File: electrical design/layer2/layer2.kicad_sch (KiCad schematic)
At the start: 36 parts, among them J1 Conn_01x01_Female, J10 Conn_01x01_Female, J2 Conn_01x01_Female, J3 Conn_01x01_Female, J4 Conn_01x01_Female, J5 Conn_01x01_Female, J6 Conn_01x01_Female, J7 Conn_01x01_Female, J8 Conn_01x01_Female, J9 Conn_01x01_Female

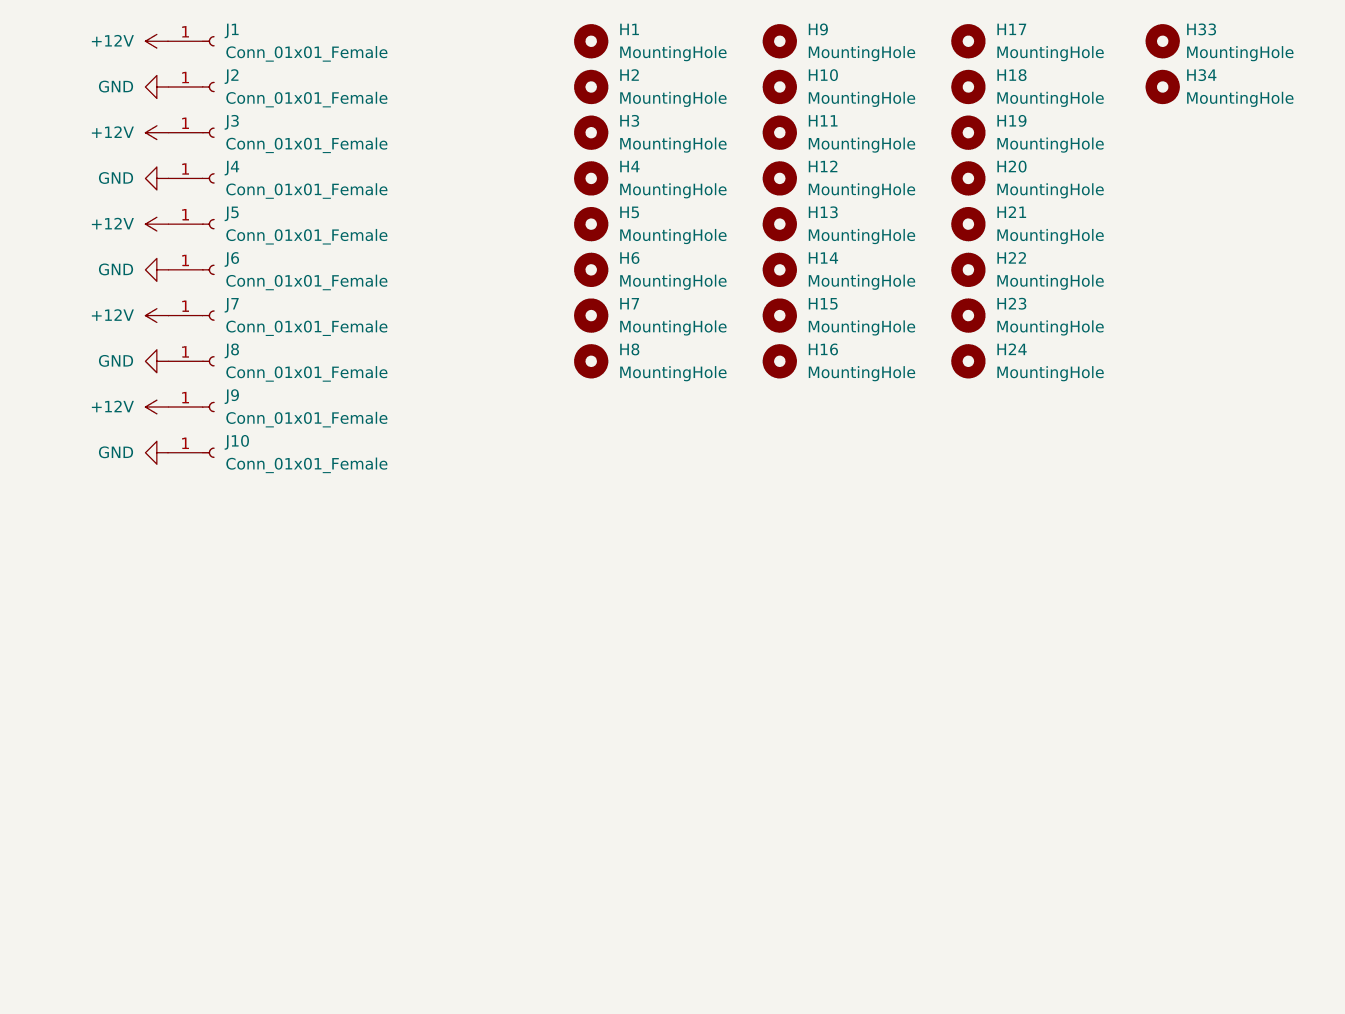
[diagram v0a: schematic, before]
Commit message: add connectors for power transfer to l3
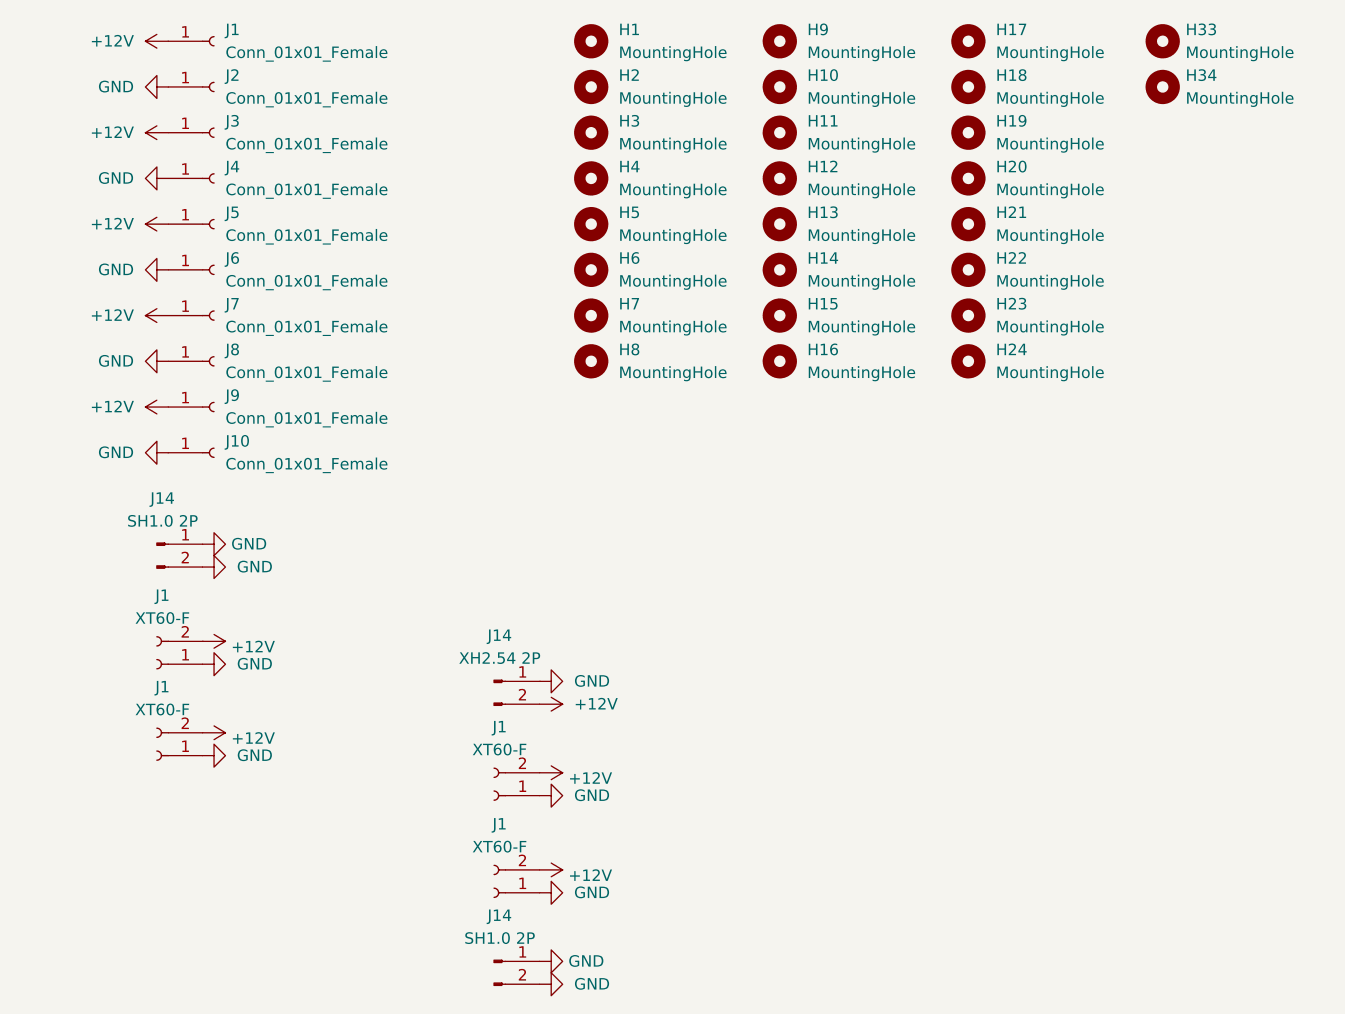
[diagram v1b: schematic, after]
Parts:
- added J1 (x3): XT60-F, Connector_AMASS:AMASS_XT30UPB-F_1x02_P5.0mm_Vertical, symbol Connector:Conn_01x02_Female
- added J1: XT60-F, Connector_AMASS:AMASS_XT30PW-F_1x02_P2.50mm_Horizontal, symbol Connector:Conn_01x02_Female
- added J14 (x2): SH1.0 2P, Connector_JST:JST_SH_SM02B-SRSS-TB_1x02-1MP_P1.00mm_Horizontal, symbol Connector:Conn_01x02_Pin
- added J14: XH2.54 2P, Connector_JST:JST_XH_B2B-XH-A_1x02_P2.50mm_Vertical, symbol Connector:Conn_01x02_Pin
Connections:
- net +12V: now also J1.2 (Pin_2), J1.2 (Pin_2), J1.2 (Pin_2), J1.2 (Pin_2), J14.2 (Pin_2)
- net GND: now also J1.1 (Pin_1), J1.1 (Pin_1), J1.1 (Pin_1), J1.1 (Pin_1), J14.1 (Pin_1), J14.1 (Pin_1), J14.1 (Pin_1), J14.2 (Pin_2), J14.2 (Pin_2)

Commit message: update pcbs and mech drawings
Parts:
- J1, J2: footprint Connector_Wire:SolderWire-2sqmm_1x01_D2mm_OD3.9mm -> Connector_Wire:SolderWire-2.5sqmm_1x01_D2.4mm_OD4.4mm
- J10, J3, J4, J5, J6, J7, J8, J9: footprint Connector_Wire:SolderWire-0.75sqmm_1x01_D1.25mm_OD2.3mm -> Connector_Wire:SolderWire-2sqmm_1x01_D2mm_OD3.9mm
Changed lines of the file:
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@@
       (effects (font (size 1.27 1.27)) (justify left))
     )
-    (property "Footprint" "Connector_Wire:SolderWire-0.75sqmm_1x01_D1.25mm_OD2.3mm" (at 38.1 60.96 0)
+    (property "Footprint" "Connector_Wire:SolderWire-2sqmm_1x01_D2mm_OD3.9mm" (at 38.1 60.96 0)
       (effects (font (size 1.27 1.27)) hide)
     )
@@
       (effects (font (size 1.27 1.27)) (justify left))
     )
-    (property "Footprint" "Connector_Wire:SolderWire-0.75sqmm_1x01_D1.25mm_OD2.3mm" (at 38.1 66.04 0)
+    (property "Footprint" "Connector_Wire:SolderWire-2sqmm_1x01_D2mm_OD3.9mm" (at 38.1 66.04 0)
       (effects (font (size 1.27 1.27)) hide)
     )
@@
       (effects (font (size 1.27 1.27)) (justify left))
     )
-    (property "Footprint" "Connector_Wire:SolderWire-0.75sqmm_1x01_D1.25mm_OD2.3mm" (at 38.1 45.72 0)
+    (property "Footprint" "Connector_Wire:SolderWire-2sqmm_1x01_D2mm_OD3.9mm" (at 38.1 45.72 0)
       (effects (font (size 1.27 1.27)) hide)
     )
@@
       (effects (font (size 1.27 1.27)) (justify left))
     )
-    (property "Footprint" "Connector_Wire:SolderWire-2sqmm_1x01_D2mm_OD3.9mm" (at 38.1 30.48 0)
+    (property "Footprint" "Connector_Wire:SolderWire-2.5sqmm_1x01_D2.4mm_OD4.4mm" (at 38.1 30.48 0)
       (effects (font (size 1.27 1.27)) hide)
     )
@@
       (effects (font (size 1.27 1.27)) (justify left))
     )
-    (property "Footprint" "Connector_Wire:SolderWire-0.75sqmm_1x01_D1.25mm_OD2.3mm" (at 38.1 35.56 0)
+    (property "Footprint" "Connector_Wire:SolderWire-2sqmm_1x01_D2mm_OD3.9mm" (at 38.1 35.56 0)
       (effects (font (size 1.27 1.27)) hide)
     )
@@
       (effects (font (size 1.27 1.27)) (justify left))
     )
-    (property "Footprint" "Connector_Wire:SolderWire-0.75sqmm_1x01_D1.25mm_OD2.3mm" (at 38.1 50.8 0)
+    (property "Footprint" "Connector_Wire:SolderWire-2sqmm_1x01_D2mm_OD3.9mm" (at 38.1 50.8 0)
       (effects (font (size 1.27 1.27)) hide)
     )
@@
       (effects (font (size 1.27 1.27)) (justify left))
     )
-    (property "Footprint" "Connector_Wire:SolderWire-2sqmm_1x01_D2mm_OD3.9mm" (at 38.1 25.4 0)
+    (property "Footprint" "Connector_Wire:SolderWire-2.5sqmm_1x01_D2.4mm_OD4.4mm" (at 38.1 25.4 0)
       (effects (font (size 1.27 1.27)) hide)
     )
@@
       (effects (font (size 1.27 1.27)) (justify left))
     )
-    (property "Footprint" "Connector_Wire:SolderWire-0.75sqmm_1x01_D1.25mm_OD2.3mm" (at 38.1 71.12 0)
+    (property "Footprint" "Connector_Wire:SolderWire-2sqmm_1x01_D2mm_OD3.9mm" (at 38.1 71.12 0)
       (effects (font (size 1.27 1.27)) hide)
     )
@@
       (effects (font (size 1.27 1.27)) (justify left))
     )
-    (property "Footprint" "Connector_Wire:SolderWire-0.75sqmm_1x01_D1.25mm_OD2.3mm" (at 38.1 40.64 0)
+    (property "Footprint" "Connector_Wire:SolderWire-2sqmm_1x01_D2mm_OD3.9mm" (at 38.1 40.64 0)
       (effects (font (size 1.27 1.27)) hide)
     )
@@
       (effects (font (size 1.27 1.27)) (justify left))
     )
-    (property "Footprint" "Connector_Wire:SolderWire-0.75sqmm_1x01_D1.25mm_OD2.3mm" (at 38.1 55.88 0)
-      (effects (font (size 1.27 1.27)) hide)
-    )
+    (property "Footprint" "Connector_Wire:SolderWire-2sqmm_1x01_D2mm_OD3.9mm" (at 38.1 55.88 0)
+      (effects (font (size 1.27 1.27)) hide)
+    )

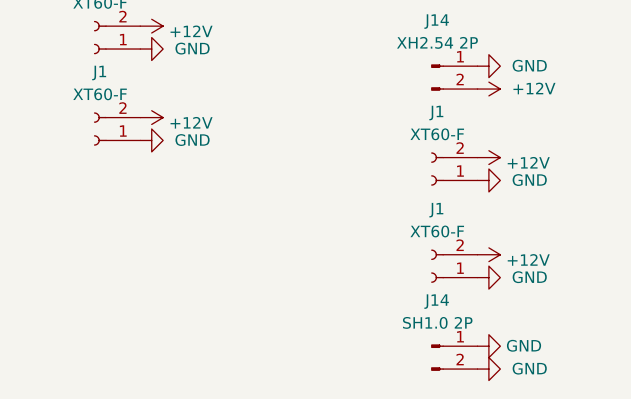
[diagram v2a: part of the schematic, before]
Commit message: update l2 pcb with additional batt connectors
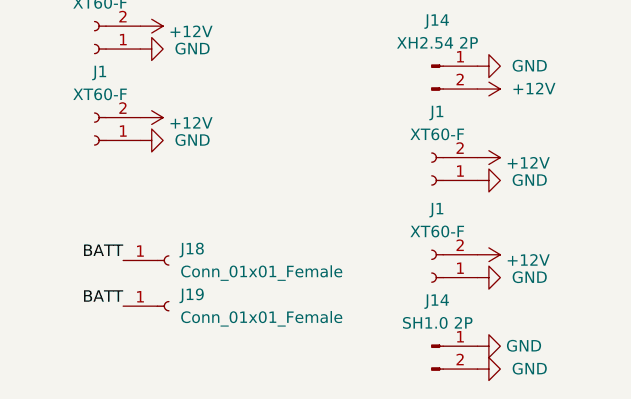
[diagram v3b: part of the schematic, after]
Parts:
- added J18, J19: Conn_01x01_Female, Connector_Wire:SolderWire-2.5sqmm_1x01_D2.4mm_OD4.4mm, symbol Connector:Conn_01x01_Female
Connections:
- new net BATT: J18.1 (Pin_1), J19.1 (Pin_1)
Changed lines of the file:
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@@
     (company "8076ducc Robotics Competition Team")
+  )
+  (label "BATT" (at 34.925 123.19 180) (fields_autoplaced)
+    (effects (font (size 1.27 1.27)) (justify right bottom))
+  )
+  (label "BATT" (at 34.925 118.11 180) (fields_autoplaced)
+    (effects (font (size 1.27 1.27)) (justify right bottom))
   )
   (symbol (lib_id "Connector:Conn_01x01_Female") (at 38.1 60.96 0) (unit 1)
@@
     )
   )
+  (symbol (lib_id "Connector:Conn_01x01_Female") (at 40.005 123.19 0) (unit 1)
+    (in_bom yes) (on_board yes) (dnp no) (fields_autoplaced)
+    (property "Reference" "J19" (at 41.275 121.9199 0)
+      (effects (font (size 1.27 1.27)) (justify left))
+    )
+    (property "Value" "Conn_01x01_Female" (at 41.275 124.4599 0)
+      (effects (font (size 1.27 1.27)) (justify left))
+    )
+    (property "Footprint" "Connector_Wire:SolderWire-2.5sqmm_1x01_D2.4mm_OD4.4mm" (at 40.005 123.19 0)
+      (effects (font (size 1.27 1.27)) hide)
+    )
+    (property "Datasheet" "~" (at 40.005 123.19 0)
+      (effects (font (size 1.27 1.27)) hide)
+    )
+    (pin "1")
+    (instances
+      (project "layer2"
+        (path "/c8578fbc-a4a8-4ef3-83ea-12d29e2f2e36"
+          (reference "J19") (unit 1)
+        )
+      )
+    )
+  )
   (symbol (lib_id "Connector:Conn_01x02_Pin") (at 69.215 96.52 0) (unit 1)
     (in_bom yes) (on_board yes) (dnp no) (fields_autoplaced)
@@
         )
       )
+    )
+  )
+  (symbol (lib_id "Connector:Conn_01x01_Female") (at 40.005 118.11 0) (unit 1)
+    (in_bom yes) (on_board yes) (dnp no) (fields_autoplaced)
+    (property "Reference" "J18" (at 41.275 116.8399 0)
+      (effects (font (size 1.27 1.27)) (justify left))
+    )
+    (property "Value" "Conn_01x01_Female" (at 41.275 119.3799 0)
+      (effects (font (size 1.27 1.27)) (justify left))
+    )
+    (property "Footprint" "Connector_Wire:SolderWire-2.5sqmm_1x01_D2.4mm_OD4.4mm" (at 40.005 118.11 0)
+      (effects (font (size 1.27 1.27)) hide)
+    )
+    (property "Datasheet" "~" (at 40.005 118.11 0)
+      (effects (font (size 1.27 1.27)) hide)
+    )
+    (pin "1")
+    (instances
+      (project "layer2"
+        (path "/c8578fbc-a4a8-4ef3-83ea-12d29e2f2e36"
+          (reference "J18") (unit 1)
+        )
+      )

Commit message: update pcbs for dual camera design
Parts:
- removed J1: XT60-F, Connector_AMASS:AMASS_XT30UPB-F_1x02_P5.0mm_Vertical, symbol Connector:Conn_01x02_Female
- removed J14: SH1.0 2P, Connector_JST:JST_SH_SM02B-SRSS-TB_1x02-1MP_P1.00mm_Horizontal, symbol Connector:Conn_01x02_Pin
- added H25, H26: MountingHole, MountingHole:MountingHole_3.2mm_M3_Pad, symbol Mechanical:MountingHole
- added J11: SH1.0 3P, Connector_JST:JST_SH_SM03B-SRSS-TB_1x03-1MP_P1.00mm_Horizontal, symbol Connector:Conn_01x03_Pin
- added J12: XH2.54 3P, Connector_JST:JST_XH_B3B-XH-A_1x03_P2.50mm_Vertical, symbol Connector:Conn_01x03_Pin
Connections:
- net +12V: now also J12.2 (Pin_2)
- net GND: now also J11.1 (Pin_1), J11.2 (Pin_2), J12.1 (Pin_1)
- new net +3V3: J11.3 (Pin_3), J12.3 (Pin_3)

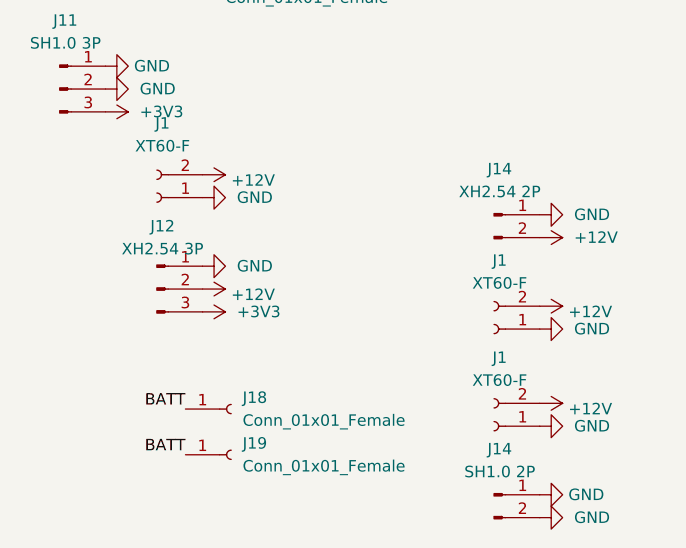
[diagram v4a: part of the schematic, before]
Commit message: add pwm pullup resistor to rpi fan connector
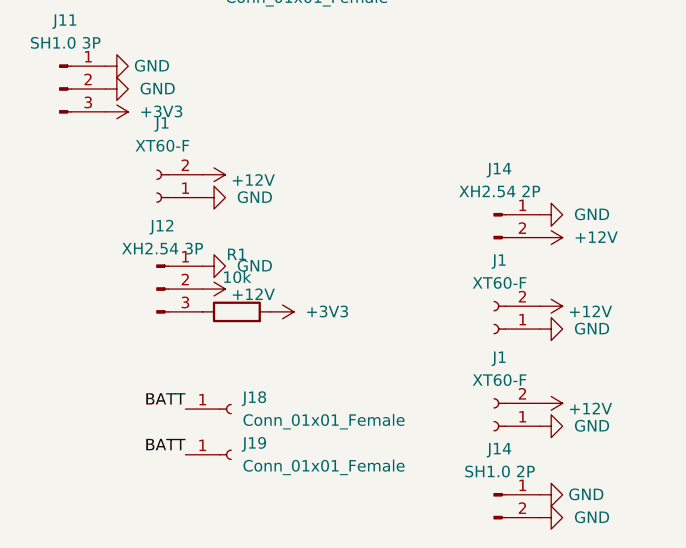
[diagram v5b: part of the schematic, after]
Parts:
- added R1: 10k, Resistor_SMD:R_0603_1608Metric, symbol Device:R
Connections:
- net +3V3: now also R1.2; no longer J12.3 (Pin_3)
- new net: J12.3 (Pin_3), R1.1
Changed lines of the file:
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@@
+    )
+  )
+  (symbol (lib_id "Device:R") (at 40.64 107.315 90) (unit 1)
+    (in_bom yes) (on_board yes) (dnp no) (fields_autoplaced)
+    (property "Reference" "R1" (at 40.64 100.965 90)
+      (effects (font (size 1.27 1.27)))
+    )
+    (property "Value" "10k" (at 40.64 103.505 90)
+      (effects (font (size 1.27 1.27)))
+    )
+    (property "Footprint" "Resistor_SMD:R_0603_1608Metric" (at 40.64 109.093 90)
+      (effects (font (size 1.27 1.27)) hide)
+    )
+    (property "Datasheet" "~" (at 40.64 107.315 0)
+      (effects (font (size 1.27 1.27)) hide)
+    )
+    (pin "2")
+    (pin "1")
+    (instances
+      (project "layer2"
+        (path "/c8578fbc-a4a8-4ef3-83ea-12d29e2f2e36"
+          (reference "R1") (unit 1)
+        )
+      )
+      (project "layer3"
+        (path "/e63e39d7-6ac0-4ffd-8aa3-1841a4541b55"
+          (reference "R8") (unit 1)
+        )
+      )
     )
   )
@@
     )
   )
-  (symbol (lib_id "power:+3V3") (at 36.83 107.315 270) (unit 1)
+  (symbol (lib_id "power:+3V3") (at 44.45 107.315 270) (unit 1)
     (in_bom yes) (on_board yes) (dnp no) (fields_autoplaced)
-    (property "Reference" "#PWR015" (at 33.02 107.315 0)
+    (property "Reference" "#PWR015" (at 40.64 107.315 0)
       (effects (font (size 1.27 1.27)) hide)
     )
-    (property "Value" "+3V3" (at 40.64 107.315 90)
+    (property "Value" "+3V3" (at 48.26 107.315 90)
       (effects (font (size 1.27 1.27)) (justify left))
     )
-    (property "Footprint" "" (at 36.83 107.315 0)
+    (property "Footprint" "" (at 44.45 107.315 0)
       (effects (font (size 1.27 1.27)) hide)
     )
-    (property "Datasheet" "" (at 36.83 107.315 0)
+    (property "Datasheet" "" (at 44.45 107.315 0)
       (effects (font (size 1.27 1.27)) hide)
     )

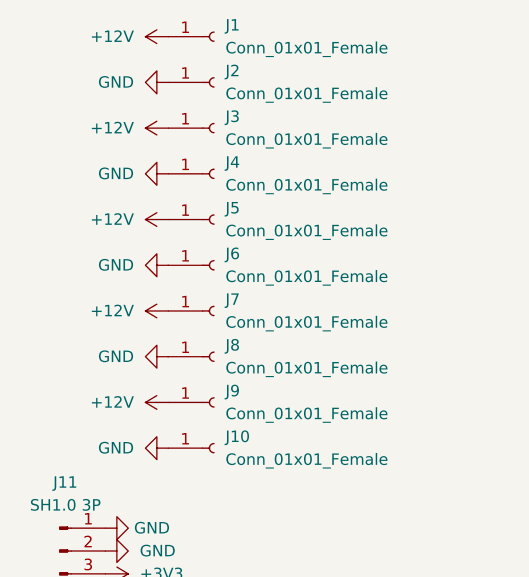
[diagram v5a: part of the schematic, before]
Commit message: reposition motor power ports
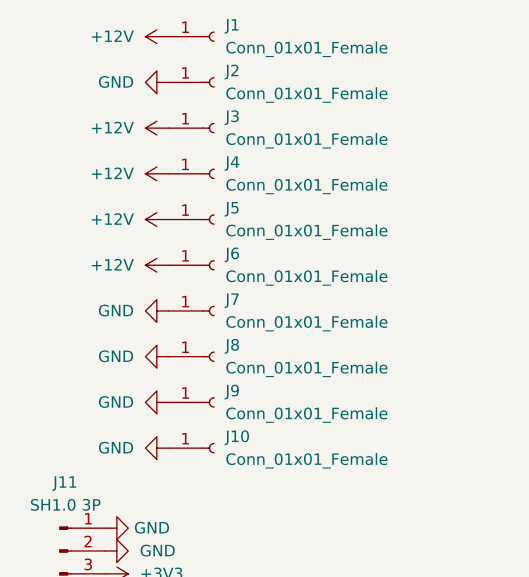
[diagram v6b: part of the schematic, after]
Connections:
- net +12V: now also J4.1 (Pin_1), J6.1 (Pin_1); no longer J7.1 (Pin_1), J9.1 (Pin_1)
- net GND: now also J7.1 (Pin_1), J9.1 (Pin_1); no longer J4.1 (Pin_1), J6.1 (Pin_1)
